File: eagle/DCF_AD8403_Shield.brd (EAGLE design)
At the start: 78.4 x 53.3 mm, 21 parts, among them IC1 NJM2732, IC2 AD8403-100

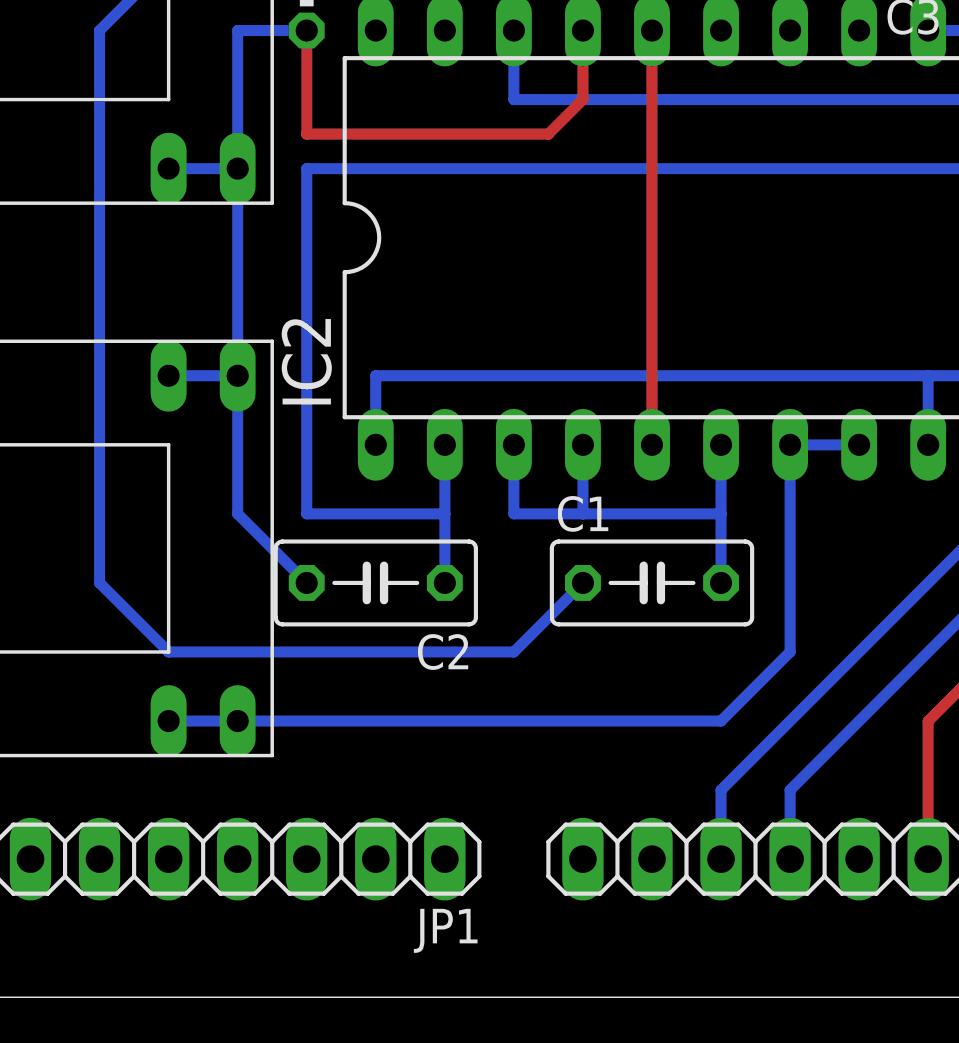
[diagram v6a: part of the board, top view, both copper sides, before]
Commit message: Add: Input trim pot
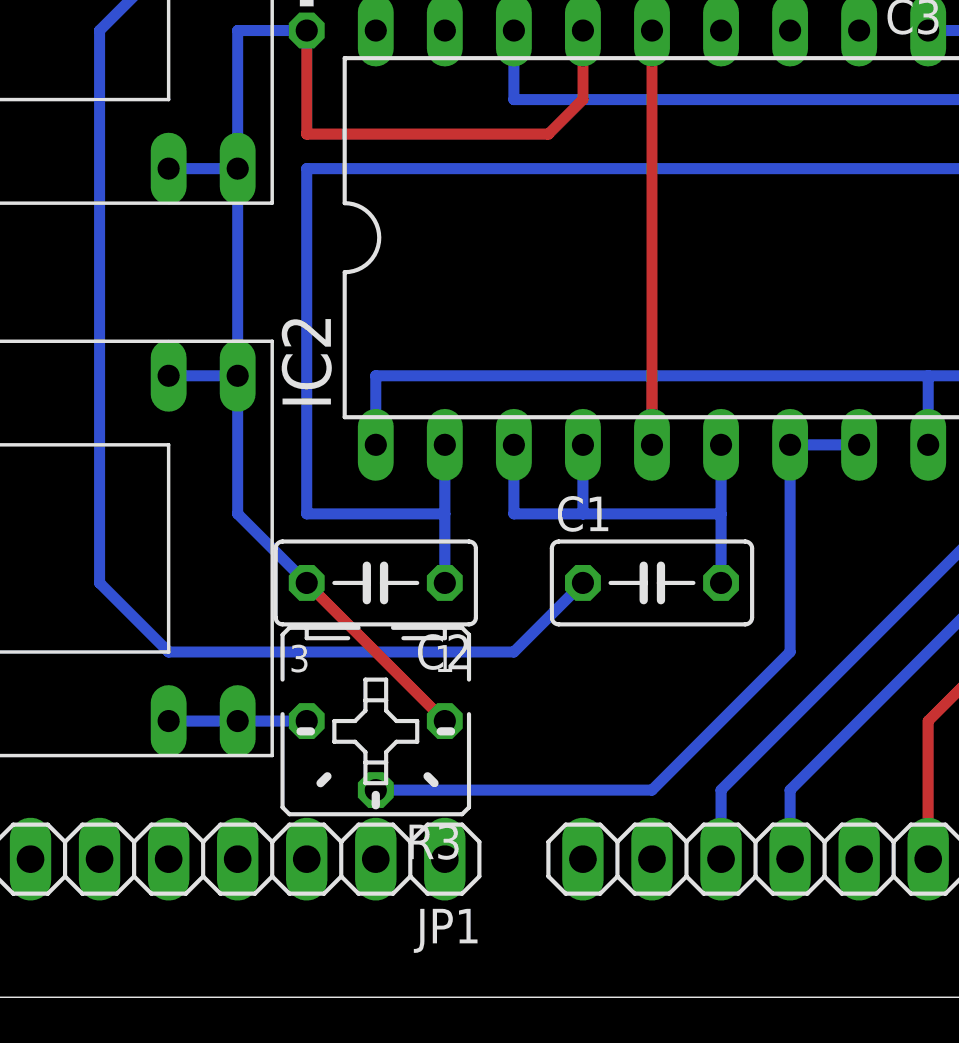
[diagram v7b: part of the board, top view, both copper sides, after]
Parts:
- added R3: (no value), pot:B25P
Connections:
- new net N$7: JK1.1, JK1.2, R3.E
- net BYPASS: now also R3.S; no longer JK1.1, JK1.2
- net N$10: now also R3.A
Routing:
- net N$10: track 126.4 -> 133.6 mm
- net BYPASS: track 34.1 -> 27.5 mm
- net N$7: track 0.00 -> 5.08 mm
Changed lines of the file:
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@@
 <element name="C4" library="rcl" package="C025-024X044" value="0.1uF" x="67.31" y="38.1" rot="R180"/>
 <element name="C5" library="rcl" package="C025-024X044" value="0.1uF" x="62.23" y="25.4" rot="R180"/>
+<element name="R3" library="pot" package="B25P" value="" x="20.32" y="10.16" rot="R180"/>
 </elements>
 <signals>
@@
 <contactref element="IC2" pad="8"/>
 <contactref element="IC2" pad="7"/>
-<contactref element="JK1" pad="1"/>
-<contactref element="JK1" pad="2"/>
-<wire x1="15.24" y1="10.16" x2="33.02" y2="10.16" width="0.4064" layer="16"/>
-<wire x1="33.02" y1="10.16" x2="35.56" y2="12.7" width="0.4064" layer="16"/>
 <wire x1="35.56" y1="12.7" x2="35.56" y2="20.32" width="0.4064" layer="16"/>
 <wire x1="35.56" y1="20.32" x2="38.1" y2="20.32" width="0.4064" layer="16"/>
-<wire x1="12.7" y1="10.16" x2="15.24" y2="10.16" width="0.4064" layer="16"/>
+<contactref element="R3" pad="S"/>
+<wire x1="20.32" y1="7.62" x2="30.48" y2="7.62" width="0.4064" layer="16"/>
+<wire x1="30.48" y1="7.62" x2="35.56" y2="12.7" width="0.4064" layer="16"/>
 </signal>
 <signal name="+5V">
@@
 </signal>
 <signal name="N$10">
-<contactref element="JK1" pad="3"/>
-<contactref element="JK1" pad="4"/>
 <contactref element="C2" pad="2"/>
 <contactref element="JK2" pad="1"/>
@@
 <wire x1="68.58" y1="30.48" x2="76.2" y2="30.48" width="0.4064" layer="16"/>
 <wire x1="17.78" y1="15.24" x2="15.24" y2="17.78" width="0.4064" layer="16"/>
-<wire x1="15.24" y1="17.78" x2="15.24" y2="22.86" width="0.4064" layer="16"/>
-<wire x1="15.24" y1="22.86" x2="15.24" y2="30.48" width="0.4064" layer="16"/>
 <wire x1="15.24" y1="30.48" x2="15.24" y2="35.56" width="0.4064" layer="16"/>
 <wire x1="15.24" y1="35.56" x2="17.78" y2="35.56" width="0.4064" layer="16"/>
 <wire x1="12.7" y1="30.48" x2="15.24" y2="30.48" width="0.4064" layer="16"/>
-<wire x1="12.7" y1="22.86" x2="15.24" y2="22.86" width="0.4064" layer="16"/>
 <wire x1="63.5" y1="25.4" x2="66.04" y2="27.94" width="0.4064" layer="16"/>
 <wire x1="66.04" y1="27.94" x2="66.04" y2="33.02" width="0.4064" layer="16"/>
@@
 <wire x1="29.21" y1="39.37" x2="27.94" y2="38.1" width="0.4064" layer="1"/>
 <wire x1="27.94" y1="38.1" x2="27.94" y2="35.56" width="0.4064" layer="1"/>
+<contactref element="JK1" pad="3"/>
+<contactref element="JK1" pad="4"/>
+<contactref element="R3" pad="A"/>
+<wire x1="15.24" y1="30.48" x2="15.24" y2="22.86" width="0.4064" layer="16"/>
+<wire x1="12.7" y1="22.86" x2="15.24" y2="22.86" width="0.4064" layer="16"/>
+<wire x1="15.24" y1="22.86" x2="15.24" y2="17.78" width="0.4064" layer="16"/>
+<wire x1="22.86" y1="10.16" x2="17.78" y2="15.24" width="0.4064" layer="1"/>
+</signal>
+<signal name="N$7">
+<contactref element="R3" pad="E"/>
+<contactref element="JK1" pad="1"/>
+<contactref element="JK1" pad="2"/>
+<wire x1="17.78" y1="10.16" x2="15.24" y2="10.16" width="0.4064" layer="16"/>
+<wire x1="15.24" y1="10.16" x2="12.7" y2="10.16" width="0.4064" layer="16"/>
 </signal>
 </signals>

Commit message: 基板図を修正
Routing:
- net GND: track 155.6 -> 156.6 mm
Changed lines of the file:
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@@
 <wire x1="25.4" y1="45.72" x2="25.4" y2="48.26" width="0.4064" layer="1"/>
 <wire x1="25.4" y1="48.26" x2="27.94" y2="48.26" width="0.4064" layer="16"/>
-<wire x1="30.48" y1="35.56" x2="30.48" y2="20.32" width="0.4064" layer="1"/>
 <wire x1="58.42" y1="40.64" x2="62.23" y2="40.64" width="0.4064" layer="1"/>
 <wire x1="62.23" y1="40.64" x2="64.77" y2="38.1" width="0.4064" layer="1"/>
 <wire x1="64.77" y1="38.1" x2="64.77" y2="26.67" width="0.4064" layer="1"/>
 <wire x1="64.77" y1="26.67" x2="66.04" y2="25.4" width="0.4064" layer="1"/>
+<wire x1="30.48" y1="35.56" x2="30.48" y2="25.4" width="0.4064" layer="1"/>
+<wire x1="30.48" y1="25.4" x2="31.75" y2="24.13" width="0.4064" layer="1"/>
+<wire x1="31.75" y1="24.13" x2="31.75" y2="21.59" width="0.4064" layer="1"/>
+<wire x1="31.75" y1="21.59" x2="30.48" y2="20.32" width="0.4064" layer="1"/>
 </signal>
 <signal name="BYPASS">
